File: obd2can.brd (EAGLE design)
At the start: 96.5 x 40.6 mm, 77 parts, among them IC1 LM339PWR, IC2 SCANTOOL, Q1 BSS138, Q2 MMBT2222, Q3 ZXMP6A13FTA, Q4 BSS138, Q5 MMBT2222, Q6 MMBT2222, Q7 8MHz, SW1 6X3.5_TACT, U1 V_REG_317SMD, U2 SN65HVD235DR, U3 MCP1700-5.0, U4 STM32F072-LQFP48, U8 MCP1700-3.3, X1 RJ45_RIGHT_ANGLEMOLEX_95001-2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, X2 RJ45_RIGHT_ANGLEMOLEX_95001-2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, Y1 16MHz

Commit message: only 5 more airwires to route...
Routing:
- net !ISO_L_TX: track 28.5 -> 58.1 mm, vias 1 -> 0
- net !ISO_K_TX: track 30.3 -> 58.2 mm, vias 1 -> 0
- net V+: track 139.9 -> 143.1 mm
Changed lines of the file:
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@@
 <setting verticaltext="up"/>
 </settings>
-<grid distance="0.001" unitdist="inch" unit="inch" style="lines" multiple="1" display="no" altdistance="0.005" altunitdist="inch" altunit="inch"/>
+<grid distance="0.01" unitdist="inch" unit="inch" style="lines" multiple="1" display="no" altdistance="0.005" altunitdist="inch" altunit="inch"/>
 <layers>
 <layer number="1" name="Top" color="4" fill="1" visible="yes" active="yes"/>
@@
 <wire x1="33.446" y1="33.48" x2="34.75" y2="33.48" width="0.254" layer="1"/>
 <wire x1="34.75" y1="33.48" x2="38.354" y2="37.084" width="0.254" layer="1"/>
-<wire x1="47.752" y1="37.338" x2="58.674" y2="37.338" width="0.254" layer="1"/>
-<wire x1="72.898" y1="20.32" x2="72.898" y2="18.288" width="0.254" layer="1"/>
-<wire x1="72.898" y1="18.288" x2="73.294" y2="17.892" width="0.254" layer="1"/>
+<wire x1="47.752" y1="37.338" x2="59.69" y2="37.338" width="0.254" layer="1"/>
 <wire x1="73.294" y1="17.892" x2="74.168" y2="17.892" width="0.254" layer="1"/>
 <wire x1="38.354" y1="37.084" x2="47.498" y2="37.084" width="0.254" layer="1"/>
 <wire x1="47.498" y1="37.084" x2="47.752" y2="37.338" width="0.254" layer="1"/>
-<via x="72.898" y="20.32" extent="1-16" drill="0.508"/>
-<wire x1="58.674" y1="37.338" x2="72.898" y2="20.32" width="0" layer="19" extent="1-1"/>
+<wire x1="59.69" y1="37.338" x2="62.738" y2="34.29" width="0.254" layer="1"/>
+<wire x1="62.738" y1="34.29" x2="62.738" y2="31.75" width="0.254" layer="1"/>
+<wire x1="62.738" y1="31.75" x2="61.214" y2="30.226" width="0.254" layer="1"/>
+<wire x1="61.214" y1="30.226" x2="61.214" y2="24.638" width="0.254" layer="1"/>
+<wire x1="61.214" y1="24.638" x2="65.532" y2="20.32" width="0.254" layer="1"/>
+<wire x1="65.532" y1="20.32" x2="70.866" y2="20.32" width="0.254" layer="1"/>
+<wire x1="70.866" y1="20.32" x2="73.294" y2="17.892" width="0.254" layer="1"/>
 </signal>
 <signal name="!ISO_L_TX">
@@
 <wire x1="33.147" y1="34.29" x2="34.925" y2="34.29" width="0.254" layer="1"/>
 <wire x1="34.925" y1="34.29" x2="38.227" y2="37.592" width="0.254" layer="1"/>
-<wire x1="74.168" y1="20.447" x2="74.168" y2="21.702" width="0.254" layer="1"/>
-<wire x1="74.295" y1="20.32" x2="74.168" y2="20.447" width="0.254" layer="1"/>
 <wire x1="47.371" y1="37.592" x2="47.625" y2="37.846" width="0.254" layer="1"/>
-<wire x1="47.625" y1="37.846" x2="57.785" y2="37.846" width="0.254" layer="1"/>
+<wire x1="47.625" y1="37.846" x2="60.198" y2="37.846" width="0.254" layer="1"/>
 <wire x1="38.227" y1="37.592" x2="47.371" y2="37.592" width="0.254" layer="1"/>
-<via x="74.295" y="20.32" extent="1-16" drill="0.508"/>
-<wire x1="57.785" y1="37.846" x2="74.168" y2="21.702" width="0" layer="19" extent="1-1"/>
+<wire x1="74.168" y1="21.702" x2="64.912" y2="21.702" width="0.254" layer="1"/>
+<wire x1="64.912" y1="21.702" x2="61.722" y2="24.892" width="0.254" layer="1"/>
+<wire x1="61.722" y1="24.892" x2="61.722" y2="29.972" width="0.254" layer="1"/>
+<wire x1="61.722" y1="29.972" x2="63.246" y2="31.496" width="0.254" layer="1"/>
+<wire x1="63.246" y1="31.496" x2="63.246" y2="34.798" width="0.254" layer="1"/>
+<wire x1="63.246" y1="34.798" x2="60.198" y2="37.846" width="0.254" layer="1"/>
 </signal>
 <signal name="RESET">
@@
 <wire x1="59.944" y1="20.804" x2="59.394" y2="20.254" width="0.254" layer="1"/>
 <wire x1="59.394" y1="20.254" x2="57.234" y2="20.254" width="0.6096" layer="1"/>
-<wire x1="60.706" y1="25.908" x2="58.928" y2="27.686" width="0.4064" layer="1"/>
-<wire x1="60.706" y1="25.908" x2="60.706" y2="21.566" width="0.4064" layer="1"/>
-<wire x1="60.706" y1="21.566" x2="59.944" y2="20.804" width="0.4064" layer="1"/>
+<wire x1="60.452" y1="26.162" x2="58.928" y2="27.686" width="0.4064" layer="1"/>
+<wire x1="60.452" y1="26.162" x2="60.452" y2="21.312" width="0.4064" layer="1"/>
+<wire x1="60.452" y1="21.312" x2="59.944" y2="20.804" width="0.4064" layer="1"/>
 </signal>
 <signal name="RST_NVM">
@@
 <wire x1="35.3568" y1="7.0104" x2="35.2776" y2="7.0104" width="0.254" layer="1"/>
 <wire x1="35.2776" y1="7.0104" x2="35.262" y2="7.026" width="0.254" layer="1"/>
-<wire x1="42.418" y1="31.877" x2="42.406" y2="34.937" width="0" layer="19" extent="1-1"/>
-<wire x1="28.448" y1="15.381" x2="27.823" y2="14.756" width="0" layer="19" extent="1-1"/>
+<wire x1="42.406" y1="34.937" x2="42.406" y2="31.75" width="0.254" layer="1"/>
+<wire x1="27.823" y1="14.756" x2="28.448" y2="15.381" width="0" layer="19" extent="1-1"/>
 </signal>
 <signal name="SWDIO">
@@
 <wire x1="76.327" y1="1.397" x2="73.802" y2="1.397" width="0.6096" layer="1"/>
 <wire x1="74.508" y1="26.162" x2="71.3584" y2="29.3116" width="0.254" layer="1"/>
-<wire x1="71.3584" y1="29.3116" x2="61.0362" y2="29.3116" width="0.254" layer="1"/>
-<via x="61.0362" y="29.3116" extent="1-16" drill="0.3556"/>
-<wire x1="61.0362" y1="29.3116" x2="60.2742" y2="30.0736" width="0.254" layer="16"/>
-<wire x1="60.2742" y1="30.0736" x2="54.4576" y2="30.0736" width="0.254" layer="16"/>
+<wire x1="71.3584" y1="29.3116" x2="62.5602" y2="29.3116" width="0.254" layer="1"/>
+<via x="62.5602" y="29.3116" extent="1-16" drill="0.3556"/>
+<wire x1="62.5602" y1="29.3116" x2="61.7982" y2="30.0736" width="0.254" layer="16"/>
+<wire x1="61.7982" y1="30.0736" x2="54.4576" y2="30.0736" width="0.254" layer="16"/>
 <via x="54.4576" y="30.0736" extent="1-16" drill="0.3556"/>
 <wire x1="54.4576" y1="30.0736" x2="53.213" y2="31.3182" width="0.254" layer="1"/>

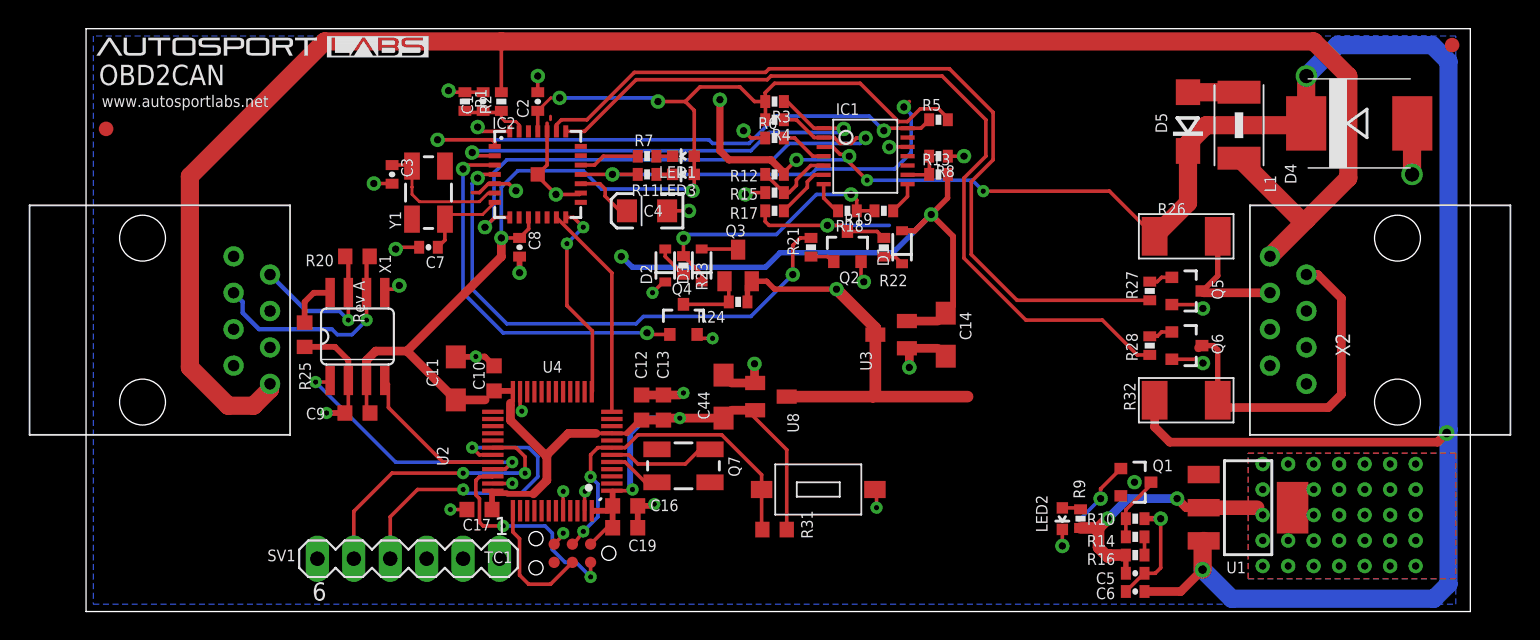
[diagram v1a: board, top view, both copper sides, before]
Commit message: fully routed; passes DRC and ERC
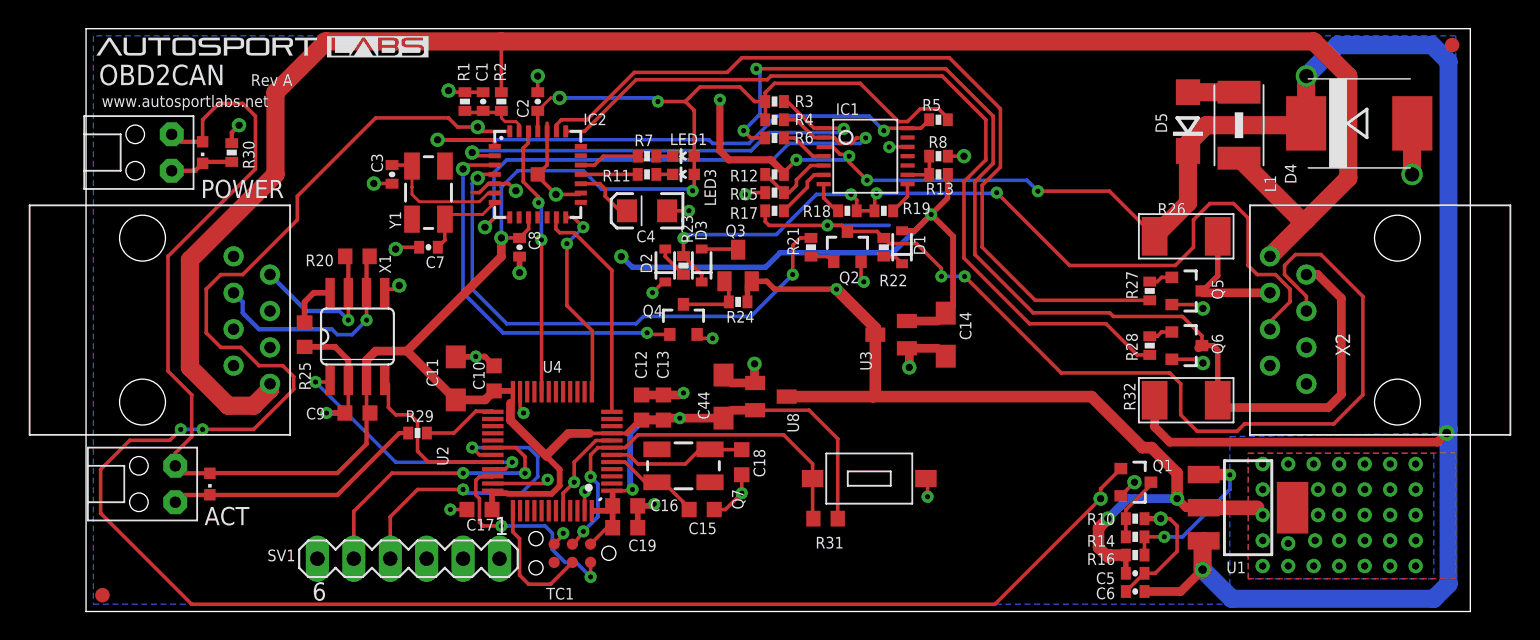
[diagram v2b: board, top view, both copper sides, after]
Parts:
- removed LED2: RED, SparkFun:LED-0603
- removed R9: 1k, SparkFun:0402-RES
- added ACT, POWER: PANEL_LED, LEDs:RIGHTANGLE_CML_5323F5
- added ACT_S, POWER_S: (no value), led:CHIPLED_0603
- added C15, C18: 0.1uf, rcl:C0603K
- added R29, R30: 180, SparkFun:0402-RES
- moved R31 3.64 mm to (51.6, 6.48)
- moved SW1 3.64 mm to (54.6, 9.27)
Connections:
- removed net AGND: U4.8
- removed net N$32: LED2.A, R9.1
- new net GND1: ACT.C, ACT_S.C, R29.1
- new net GND2: POWER.C, POWER_S.C, R30.1
- new net N$11: R29.2, U4.25
- net GND: now also C15.1, C18.1, R30.2, U4.8; no longer LED2.C
- net N$40: now also C18.2
- net N$42: now also C15.2
- net RESET_STN: now also U4.20
- net V+: now also ACT.A, ACT_S.A, POWER.A, POWER_S.A
- net VCC: no longer R9.2
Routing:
- net PWM/!VPW: track 7.20 -> 135.7 mm, vias 2 -> 4
- net J1850BUS-: track 13.8 -> 73.1 mm, vias 1 -> 3
- net V+: track 143.1 -> 200.6 mm
- net K-LINE: track 25.8 -> 77.6 mm, vias 1 -> 2
- net J1850BUS+: track 19.1 -> 62.0 mm, vias 2 -> 4
- net RST_NVM: track 29.4 -> 3.98 mm, vias 2 -> 0
- net RESET_STN: track 0.00 -> 18.8 mm, vias 0 -> 2
- net GND1: track 0.00 -> 18.3 mm
- net VCC: track 47.3 -> 64.7 mm
- net GND: track 80.8 -> 95.5 mm, vias 34 -> 35
- net N$8: track 1.29 -> 11.5 mm, vias 0 -> 2
- net N$11: track 0.00 -> 5.25 mm
- net GND2: track 0.00 -> 4.45 mm
- net RESET: track 24.9 -> 28.1 mm
- net N$42: track 3.73 -> 6.83 mm
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
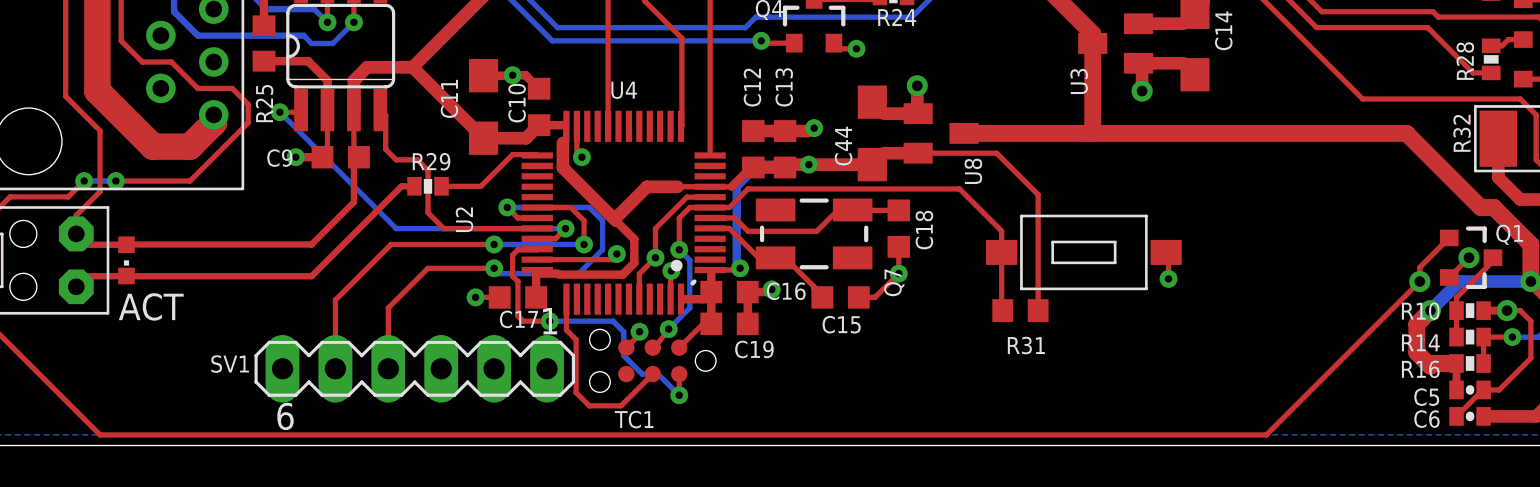
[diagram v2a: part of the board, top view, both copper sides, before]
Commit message: added the ability to supply power via FTDI header
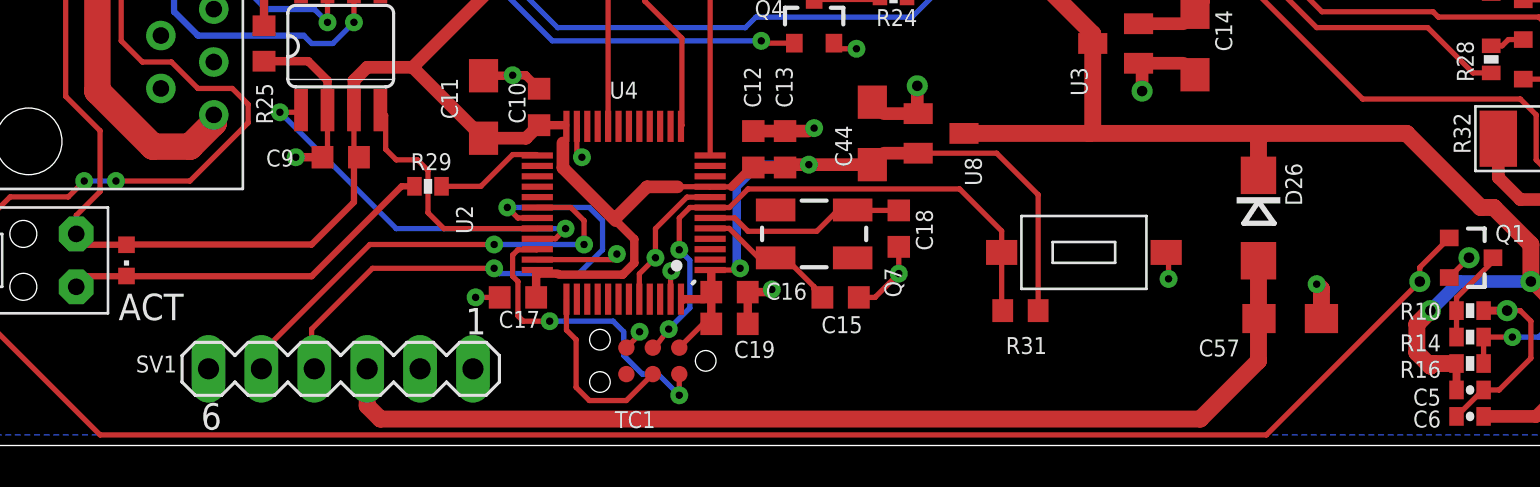
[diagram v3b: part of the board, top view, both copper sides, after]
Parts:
- added C57: 10uF, rcl:SMC_A
- added D26: SCHOTTKY, smt_diodes:SMA
- moved SV1 3.56 mm to (18.9, 3.68)
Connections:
- removed net +5V: SV1.3
- new net VBUS: C57.+, D26.A, SV1.3
- net GND: now also C57.-
- net VCC: now also D26.C
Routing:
- net VBUS: track 0.00 -> 50.8 mm
- net USART1_RX: track 22.5 -> 25.6 mm
- net VCC: track 64.7 -> 66.8 mm
- net USART1_TX: track 20.0 -> 22.1 mm
- net GND: track 95.5 -> 97.3 mm, vias 35 -> 36
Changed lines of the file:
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@@
 <setting verticaltext="up"/>
 </settings>
-<grid distance="0.002" unitdist="inch" unit="inch" style="lines" multiple="1" display="no" altdistance="0.005" altunitdist="inch" altunit="inch"/>
+<grid distance="0.01" unitdist="inch" unit="inch" style="lines" multiple="1" display="no" altdistance="0.005" altunitdist="inch" altunit="inch"/>
 <layers>
 <layer number="1" name="Top" color="4" fill="1" visible="yes" active="yes"/>
@@
 <attribute name="NAME" x="24.552" y="15.672" size="0.8128" layer="25" rot="R90"/>
 </element>
-<element name="SV1" library="con-lstb" package="MA06-1" value="" x="22.479" y="3.683" smashed="yes" rot="R180">
-<attribute name="OC_NEWARK" value="unknown" x="22.479" y="3.683" size="0.8128" layer="27" rot="R180" display="off"/>
-<attribute name="MPN" value="" x="22.479" y="3.683" size="0.8128" layer="27" rot="R180" display="off"/>
-<attribute name="MF" value="" x="22.479" y="3.683" size="0.8128" layer="27" rot="R180" display="off"/>
-<attribute name="OC_FARNELL" value="unknown" x="22.479" y="3.683" size="0.8128" layer="27" rot="R180" display="off"/>
-<attribute name="NAME" x="14.605" y="4.318" size="0.8128" layer="25" ratio="10" rot="R180"/>
-<attribute name="VALUE" x="25.019" y="6.604" size="1.27" layer="27" ratio="10" rot="R180"/>
+<element name="SV1" library="con-lstb" package="MA06-1" value="" x="18.923" y="3.683" smashed="yes" rot="R180">
+<attribute name="OC_NEWARK" value="unknown" x="18.923" y="3.683" size="0.8128" layer="27" rot="R180" display="off"/>
+<attribute name="MPN" value="" x="18.923" y="3.683" size="0.8128" layer="27" rot="R180" display="off"/>
+<attribute name="MF" value="" x="18.923" y="3.683" size="0.8128" layer="27" rot="R180" display="off"/>
+<attribute name="OC_FARNELL" value="unknown" x="18.923" y="3.683" size="0.8128" layer="27" rot="R180" display="off"/>
+<attribute name="NAME" x="11.049" y="4.318" size="0.8128" layer="25" ratio="10" rot="R180"/>
+<attribute name="VALUE" x="21.463" y="6.604" size="1.27" layer="27" ratio="10" rot="R180"/>
 </element>
 <element name="SW1" library="tactile_switch" package="TACT_6X3.5" value="6X3.5_TACT" x="54.61" y="9.271" smashed="yes"/>
@@
 <attribute name="NAME" x="8.001" y="28.829" size="1.27" layer="21"/>
 </element>
+<element name="C57" library="rcl" package="SMC_A" value="10uF" x="64.516" y="6.096" smashed="yes">
+<attribute name="NAME" x="60.122" y="4.277" size="0.8128" layer="25"/>
+</element>
+<element name="D26" library="smt_diodes" package="SMA" value="SCHOTTKY" x="62.992" y="10.922" smashed="yes" rot="R270">
+<attribute name="NAME" x="64.278" y="13.562" size="0.8128" layer="25" ratio="10" rot="R270"/>
+</element>
 </elements>
 <signals>
@@
 <wire x1="35.548" y1="11.926" x2="34.036" y2="10.414" width="0.254" layer="1"/>
 <wire x1="34.036" y1="10.414" x2="34.036" y2="9.017" width="0.254" layer="1"/>
+<contactref element="C57" pad="-"/>
+<via x="65.786" y="7.747" extent="1-16" drill="0.3556"/>
+<wire x1="66.016" y1="6.096" x2="66.016" y2="7.517" width="0.8128" layer="1"/>
+<wire x1="66.016" y1="7.517" x2="65.786" y2="7.747" width="0.8128" layer="1"/>
 </signal>
 <signal name="!VPW_RX">
@@
 <wire x1="70.597" y1="5.827" x2="70.597" y2="4.46" width="0.8128" layer="1"/>
 <wire x1="70.597" y1="4.46" x2="71.247" y2="3.81" width="0.8128" layer="1"/>
-<wire x1="54.864" y1="14.986" x2="70.104" y2="14.986" width="0.8128" layer="1"/>
+<wire x1="54.864" y1="14.986" x2="63.246" y2="14.986" width="0.8128" layer="1"/>
+<wire x1="63.246" y1="14.986" x2="70.104" y2="14.986" width="0.8128" layer="1"/>
 <wire x1="70.104" y1="14.986" x2="73.66" y2="11.43" width="0.8128" layer="1"/>
 <wire x1="73.66" y1="11.43" x2="74.295" y2="11.43" width="0.8128" layer="1"/>
 <wire x1="74.295" y1="11.43" x2="76.073" y2="9.652" width="0.8128" layer="1"/>
 <wire x1="76.073" y1="9.652" x2="76.073" y2="7.874" width="0.8128" layer="1"/>
+<contactref element="D26" pad="C"/>
+<wire x1="62.992" y1="12.972" x2="62.992" y2="14.732" width="0.8128" layer="1"/>
+<wire x1="62.992" y1="14.732" x2="63.246" y2="14.986" width="0.8128" layer="1"/>
 </signal>
 <signal name="N$9">
@@
 <wire x1="39.766" y1="30.48" x2="40.906" y2="30.48" width="0.254" layer="1"/>
 </signal>
-<signal name="+5V">
-<contactref element="SV1" pad="3"/>
-</signal>
 <signal name="CANL">
 <contactref element="U2" pad="6"/>
@@
 <contactref element="U4" pad="37"/>
 <contactref element="TC1" pad="4"/>
-<wire x1="33.909" y1="3.429" x2="32.385" y2="1.905" width="0.254" layer="1"/>
-<wire x1="32.385" y1="1.905" x2="30.861" y2="1.905" width="0.254" layer="1"/>
-<wire x1="30.861" y1="1.905" x2="30.226" y2="2.54" width="0.254" layer="1"/>
-<wire x1="30.226" y1="2.54" x2="30.226" y2="5.08" width="0.254" layer="1"/>
+<wire x1="33.909" y1="3.429" x2="32.639" y2="2.159" width="0.254" layer="1"/>
+<wire x1="32.639" y1="2.159" x2="30.861" y2="2.159" width="0.254" layer="1"/>
+<wire x1="30.861" y1="2.159" x2="30.226" y2="2.794" width="0.254" layer="1"/>
+<wire x1="30.226" y1="2.794" x2="30.226" y2="5.08" width="0.254" layer="1"/>
 <wire x1="29.762" y1="7.026" x2="29.762" y2="5.544" width="0.254" layer="1"/>
 <wire x1="29.762" y1="5.544" x2="30.226" y2="5.08" width="0.254" layer="1"/>
@@
 <wire x1="30.607" y1="9.652" x2="26.289" y2="9.652" width="0.254" layer="16"/>
 <via x="26.289" y="9.652" extent="1-16" drill="0.3556"/>
-<wire x1="26.289" y1="9.652" x2="21.336" y2="9.652" width="0.254" layer="1"/>
-<wire x1="21.336" y1="9.652" x2="18.669" y2="6.985" width="0.254" layer="1"/>
-<wire x1="18.669" y1="6.985" x2="18.669" y2="3.683" width="0.254" layer="1"/>
+<wire x1="26.289" y1="9.652" x2="20.32" y2="9.652" width="0.254" layer="1"/>
+<wire x1="20.32" y1="9.652" x2="15.24" y2="4.572" width="0.254" layer="1"/>
+<wire x1="15.24" y1="4.572" x2="15.24" y2="3.81" width="0.254" layer="1"/>
+<wire x1="15.24" y1="3.81" x2="15.113" y2="3.683" width="0.254" layer="1"/>
 </signal>
 <signal name="USART1_RX">
@@
 <wire x1="26.543" y1="8.255" x2="26.289" y2="8.509" width="0.254" layer="16"/>
 <via x="26.289" y="8.509" extent="1-16" drill="0.3556"/>
-<wire x1="26.289" y1="8.509" x2="23.114" y2="8.509" width="0.254" layer="1"/>
-<wire x1="23.114" y1="8.509" x2="21.209" y2="6.604" width="0.254" layer="1"/>
-<wire x1="21.209" y1="6.604" x2="21.209" y2="3.683" width="0.254" layer="1"/>
+<wire x1="26.289" y1="8.509" x2="20.447" y2="8.509" width="0.254" layer="1"/>
+<wire x1="20.447" y1="8.509" x2="17.526" y2="5.588" width="0.254" layer="1"/>
+<wire x1="17.526" y1="5.588" x2="17.526" y2="3.81" width="0.254" layer="1"/>
+<wire x1="17.526" y1="3.81" x2="17.653" y2="3.683" width="0.254" layer="1"/>
 </signal>
 <signal name="ANALOG_1_ADC">
@@
 <wire x1="8.228" y1="31.354" x2="8.128" y2="31.254" width="0.3048" layer="1"/>
 </signal>
+<signal name="VBUS">
+<contactref element="C57" pad="+"/>
+<contactref element="D26" pad="A"/>
+<contactref element="SV1" pad="3"/>
+<wire x1="62.992" y1="8.872" x2="62.992" y2="6.12" width="0.8128" layer="1"/>
+<wire x1="62.992" y1="6.12" x2="63.016" y2="6.096" width="0.8128" layer="1"/>
+<wire x1="20.193" y1="3.683" x2="20.193" y2="1.905" width="0.8128" layer="1"/>
+<wire x1="20.193" y1="1.905" x2="20.828" y2="1.27" width="0.8128" layer="1"/>
+<wire x1="20.828" y1="1.27" x2="60.198" y2="1.27" width="0.8128" layer="1"/>
+<wire x1="60.198" y1="1.27" x2="62.992" y2="4.064" width="0.8128" layer="1"/>
+<wire x1="62.992" y1="4.064" x2="62.992" y2="6.072" width="0.8128" layer="1"/>
+<wire x1="62.992" y1="6.072" x2="63.016" y2="6.096" width="0.8128" layer="1"/>
+</signal>
 </signals>
